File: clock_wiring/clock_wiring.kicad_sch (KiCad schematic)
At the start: 38 parts, among them J1 Conn_01x01_Female, J2 Conn_01x01_Female, J3 Conn_01x01_Female, J4 Conn_01x01_Female, J5 Conn_01x01_Female, J6 Conn_01x01_Female, J8 Conn_01x01_Female, SW1 SW_Push, SW2 SW_Push, SW3 SW_Push, SW4 SW_Push, U1 ATmega328-P, U2 74HC595, U3 COM-09481, U4 AVR-ISP-6, U5 TinyRTC, Y1 Crystal

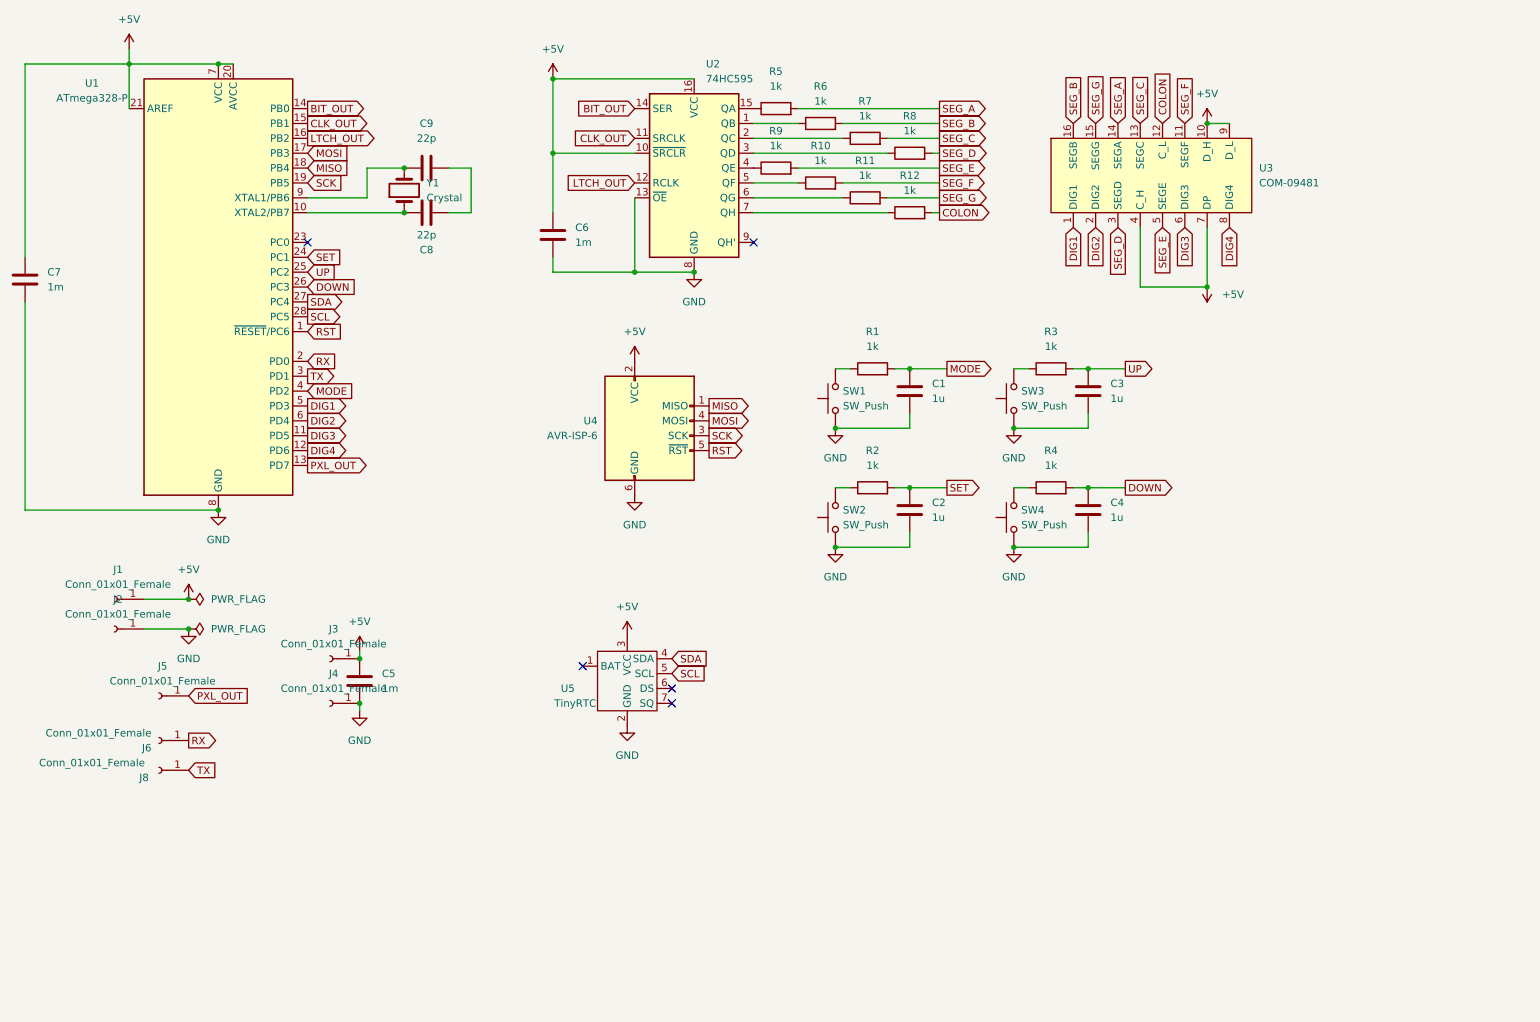
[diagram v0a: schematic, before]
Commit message: Add traces for all signals, power on plane
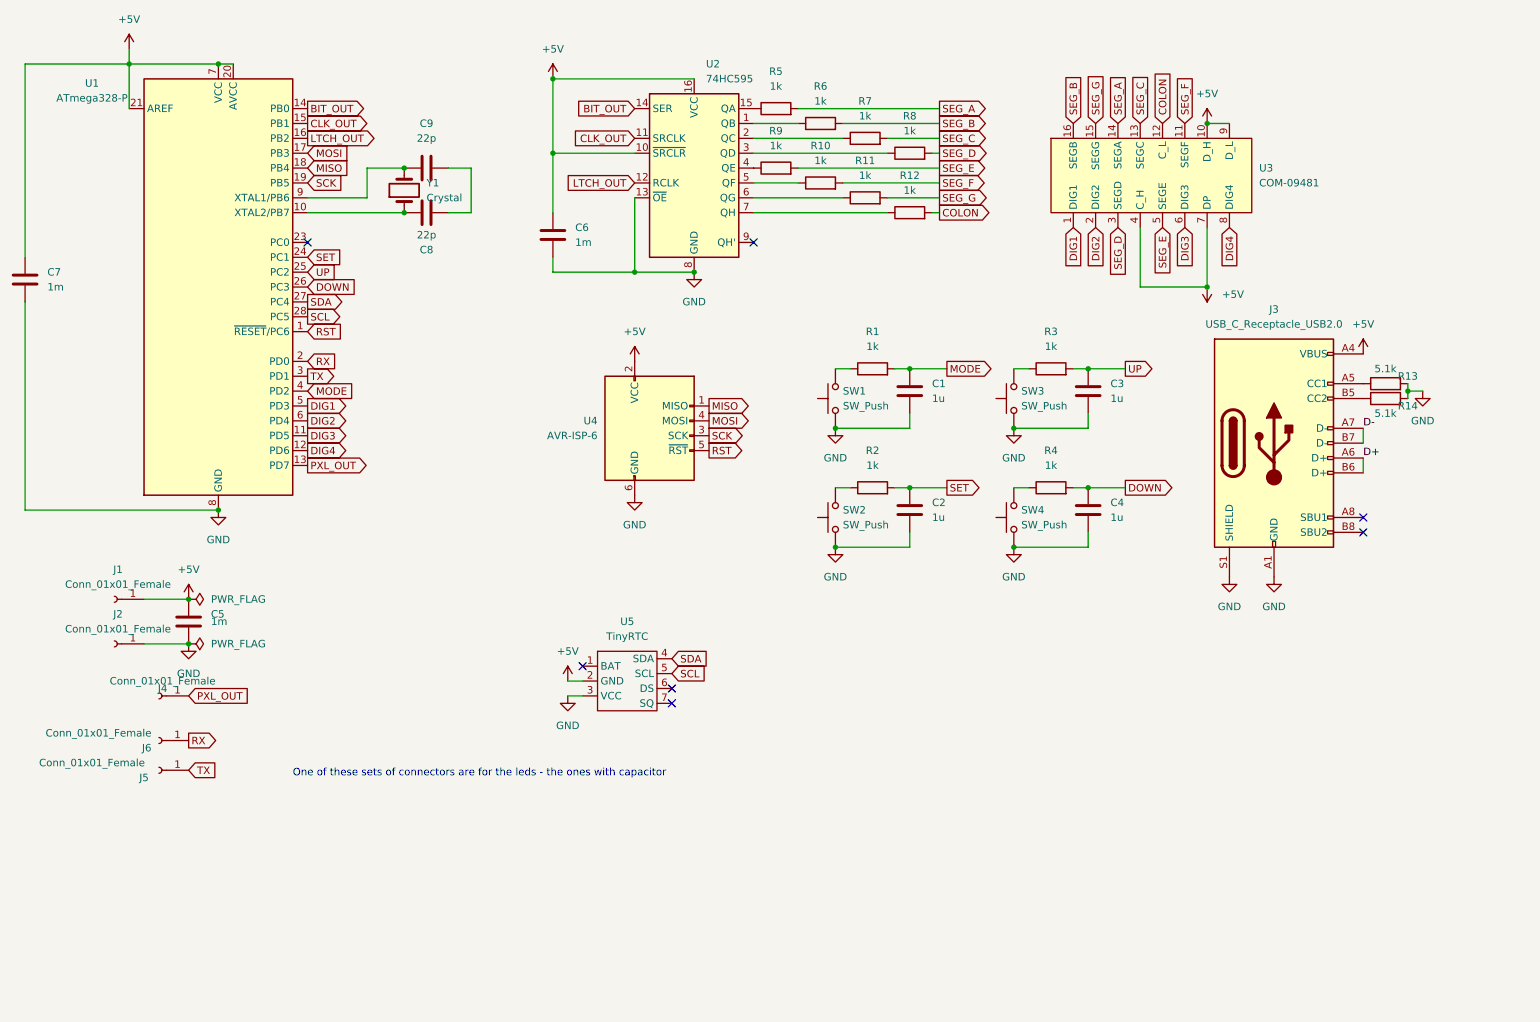
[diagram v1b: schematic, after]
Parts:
- removed J3, J4: Conn_01x01_Female, Connector_Pin:Pin_D1.0mm_L10.0mm_LooseFit, symbol Connector:Conn_01x01_Female
- added J3: USB_C_Receptacle_USB2.0, Connector_USB:USB_C_Receptacle_Palconn_UTC16-G, symbol Connector:USB_C_Receptacle_USB2.0
- added R13, R14: 5.1k, Resistor_SMD:R_1206_3216Metric_Pad1.30x1.75mm_HandSolder, symbol Device:R
- renumbered J5 to J4, J8 to J5
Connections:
- net +5V: now also U5.2 (GND), J3.A4 (VBUS), J3.A9 (VBUS), J3.B4 (VBUS), J3.B9 (VBUS); no longer U5.3 (VCC)
- net GND: now also U5.3 (VCC), J3.A1 (GND), J3.A12 (GND), J3.B1 (GND), J3.B12 (GND), J3.S1 (SHIELD), R13.2, R14.2; no longer U5.2 (GND)
- new net: J3.A5 (CC1), R13.1
- new net: J3.B5 (CC2), R14.1
- new net D+: J3.A6 (D+), J3.B6 (D+)
- new net D-: J3.A7 (D-), J3.B7 (D-)
- no-connect marks 5 -> 7
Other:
- note added: "One of these sets of connectors are for the leds - the ones with capacitor"
- moved on the sheet: J2

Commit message: update pcb ground plane(s), power trace, via/trace connections, fix pin sizes, notes in schematic on improvements to add
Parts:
- added D? (x2): LED, symbol Device:LED
- added F?: Polyfuse, symbol Device:Polyfuse
- added R? (x2): R, symbol Device:R
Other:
- note added: "Check the order of gnd and vcc pins (get ref sheet again) Add placeholder pin outputs for the DS and SQ"
- note added: "Connect one LED straight to power, one to pin23 for an RTC status pin Wire up the PTC (polyfuse)"
- note added: "check tiny rtc pins (gnd and v may be wswapped) pull up on sda and scl (3v3?) - check pull up resistor docs for it) ground plane fill (maybe on back too + stitch with vias) DONE + this may allow some via cleanup DONE 2m -> 2.54m header DONE round edges of pcb ptc fuse status leds (power on, rtc up)"
- note added: "usb distance to edge (closer) DONE"
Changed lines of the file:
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@@
     (stroke (width 0) (type default) (color 0 0 0 0))
+  )
+  (text "usb distance to edge (closer) DONE\n" (at 30.48 191.77 0)
+    (effects (font (size 1.27 1.27)) (justify left bottom))
+  )
+  (text "Check the order of gnd and vcc pins (get ref sheet again)\nAdd placeholder pin outputs for the DS and SQ"
+    (at 104.14 124.46 0)
+    (effects (font (size 1.27 1.27)) (justify left bottom))
   )
   (text "One of these sets of connectors are for the leds - the ones with capacitor"
     (at 60.96 152.4 0)
+    (effects (font (size 1.27 1.27)) (justify left bottom))
+  )
+  (text "Connect one LED straight to power, one to pin23 for an RTC status pin\nWire up the PTC (polyfuse)"
+    (at 187.96 146.05 0)
+    (effects (font (size 1.27 1.27)) (justify left bottom))
+  )
+  (text "check tiny rtc pins (gnd and v may be wswapped)\npull up on sda and scl (3v3?) - check pull up resistor docs for it)\nground plane fill (maybe on back too + stitch with vias) DONE\n+ this may allow some via cleanup DONE\n2m -> 2.54m header DONE\nround edges of pcb\nptc fuse\nstatus leds (power on, rtc up)"
+    (at 19.05 182.88 0)
     (effects (font (size 1.27 1.27)) (justify left bottom))
   )
@@
     (pin "2")
   )
+  (symbol (lib_id "Device:LED") (at 170.18 148.59 0) (unit 1)
+    (in_bom yes) (on_board yes) (fields_autoplaced)
+    (property "Reference" "D?" (id 0) (at 168.5925 142.24 0))
+    (property "Value" "LED" (id 1) (at 168.5925 144.78 0))
+    (property "Footprint" "" (id 2) (at 170.18 148.59 0)
+      (effects (font (size 1.27 1.27)) hide)
+    )
+    (property "Datasheet" "~" (id 3) (at 170.18 148.59 0)
+      (effects (font (size 1.27 1.27)) hide)
+    )
+    (pin "1")
+    (pin "2")
+  )
   (symbol (lib_id "Device:R") (at 158.75 53.34 90) (unit 1)
     (in_bom yes) (on_board yes) (fields_autoplaced)
@@
     (pin "2")
   )
+  (symbol (lib_id "Device:R") (at 184.15 157.48 0) (unit 1)
+    (in_bom yes) (on_board yes) (fields_autoplaced)
+    (property "Reference" "R?" (id 0) (at 186.69 156.2099 0)
+      (effects (font (size 1.27 1.27)) (justify left))
+    )
+    (property "Value" "R" (id 1) (at 186.69 158.7499 0)
+      (effects (font (size 1.27 1.27)) (justify left))
+    )
+    (property "Footprint" "" (id 2) (at 182.372 157.48 90)
+      (effects (font (size 1.27 1.27)) hide)
+    )
+    (property "Datasheet" "~" (id 3) (at 184.15 157.48 0)
+      (effects (font (size 1.27 1.27)) hide)
+    )
+    (pin "1")
+    (pin "2")
+  )
   (symbol (lib_id "Connector:Conn_01x01_Female") (at 30.48 121.92 180) (unit 1)
     (in_bom yes) (on_board yes) (fields_autoplaced)
@@
     )
     (pin "1")
+  )
+  (symbol (lib_id "Device:Polyfuse") (at 190.5 134.62 0) (unit 1)
+    (in_bom yes) (on_board yes) (fields_autoplaced)
+    (property "Reference" "F?" (id 0) (at 193.04 133.3499 0)
+      (effects (font (size 1.27 1.27)) (justify left))
+    )
+    (property "Value" "Polyfuse" (id 1) (at 193.04 135.8899 0)
+      (effects (font (size 1.27 1.27)) (justify left))
+    )
+    (property "Footprint" "" (id 2) (at 191.77 139.7 0)
+      (effects (font (size 1.27 1.27)) (justify left) hide)
+    )
+    (property "Datasheet" "~" (id 3) (at 190.5 134.62 0)
+      (effects (font (size 1.27 1.27)) hide)
+    )
+    (pin "1")
+    (pin "2")
   )
   (symbol (lib_id "power:GND") (at 184.15 92.71 0) (unit 1)
@@
     )
     (pin "1")
+    (pin "2")
+    (pin "3")
+    (pin "4")
+    (pin "5")
     (pin "6")
-    (pin "2")
-    (pin "5")
-    (pin "4")
     (pin "7")
-    (pin "3")
   )
   (symbol (lib_id "power:+5V") (at 217.17 68.58 180) (unit 1)
@@
     )
     (pin "1")
+  )
+  (symbol (lib_id "Device:R") (at 170.18 157.48 0) (unit 1)
+    (in_bom yes) (on_board yes) (fields_autoplaced)
+    (property "Reference" "R?" (id 0) (at 172.72 156.2099 0)
+      (effects (font (size 1.27 1.27)) (justify left))
+    )
+    (property "Value" "R" (id 1) (at 172.72 158.7499 0)
+      (effects (font (size 1.27 1.27)) (justify left))
+    )
+    (property "Footprint" "" (id 2) (at 168.402 157.48 90)
+      (effects (font (size 1.27 1.27)) hide)
+    )
+    (property "Datasheet" "~" (id 3) (at 170.18 157.48 0)
+      (effects (font (size 1.27 1.27)) hide)
+    )
+    (pin "1")
+    (pin "2")
   )
   (symbol (lib_id "Connector:Conn_01x01_Female") (at 38.1 146.05 180) (unit 1)
@@
     (pin "1")
   )
+  (symbol (lib_id "Device:LED") (at 185.42 148.59 0) (unit 1)
+    (in_bom yes) (on_board yes) (fields_autoplaced)
+    (property "Reference" "D?" (id 0) (at 183.8325 142.24 0))
+    (property "Value" "LED" (id 1) (at 183.8325 144.78 0))
+    (property "Footprint" "" (id 2) (at 185.42 148.59 0)
+      (effects (font (size 1.27 1.27)) hide)
+    )
+    (property "Datasheet" "~" (id 3) (at 185.42 148.59 0)
+      (effects (font (size 1.27 1.27)) hide)
+    )
+    (pin "1")
+    (pin "2")
+  )
   (symbol (lib_id "Device:R") (at 166.37 55.88 90) (unit 1)
     (in_bom yes) (on_board yes) (fields_autoplaced)
@@
       (reference "C9") (unit 1) (value "22p") (footprint "Capacitor_SMD:C_1206_3216Metric_Pad1.33x1.80mm_HandSolder")
     )
+    (path "/2c80991e-594d-4eee-96e9-39636dcb7ee0"
+      (reference "D?") (unit 1) (value "LED") (footprint "")
+    )
+    (path "/f3706809-b8a4-40d6-9e53-0a622adc468d"
+      (reference "D?") (unit 1) (value "LED") (footprint "")
+    )
+    (path "/5be3c29e-1d4e-4508-94f2-d66ac40d766d"
+      (reference "F?") (unit 1) (value "Polyfuse") (footprint "")
+    )
     (path "/3dd50d09-95c5-49e1-a60e-2c84ac6d0e3a"
       (reference "J1") (unit 1) (value "Conn_01x01_Female") (footprint "Connector_Pin:Pin_D1.0mm_L10.0mm_LooseFit")
@@
       (reference "R14") (unit 1) (value "5.1k") (footprint "Resistor_SMD:R_1206_3216Metric_Pad1.30x1.75mm_HandSolder")
     )
+    (path "/3474a408-f361-447c-8f87-a5fd9f64fc61"
+      (reference "R?") (unit 1) (value "R") (footprint "")
+    )
+    (path "/9b1571b5-cdeb-4949-b2f4-a2ed131b1042"
+      (reference "R?") (unit 1) (value "R") (footprint "")
+    )
     (path "/65450cb2-84a4-4591-b0b0-816bff153040"
